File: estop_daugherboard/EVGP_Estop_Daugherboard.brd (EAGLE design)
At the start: 82.6 x 94.1 mm, 41 parts, among them J1 JST-XH-02-PIN-LONG-PAD, J2 JST-XH-02-PIN-LONG-PAD, J3 JST-XH-03-PIN-LONG-PAD, J4 JST-XH-03-PIN-LONG-PAD, J5 AVR_SPI_PROG_3X2PTH, J6 UX60-MB-5S8, J7 4_XH_JST, Q1 N_FET2, Q2 N_FET1, U1 NL27WZ08USG, U2 ATMEGA32U4-AU, X1 TSX-3225 16.0000MF18X-AC0

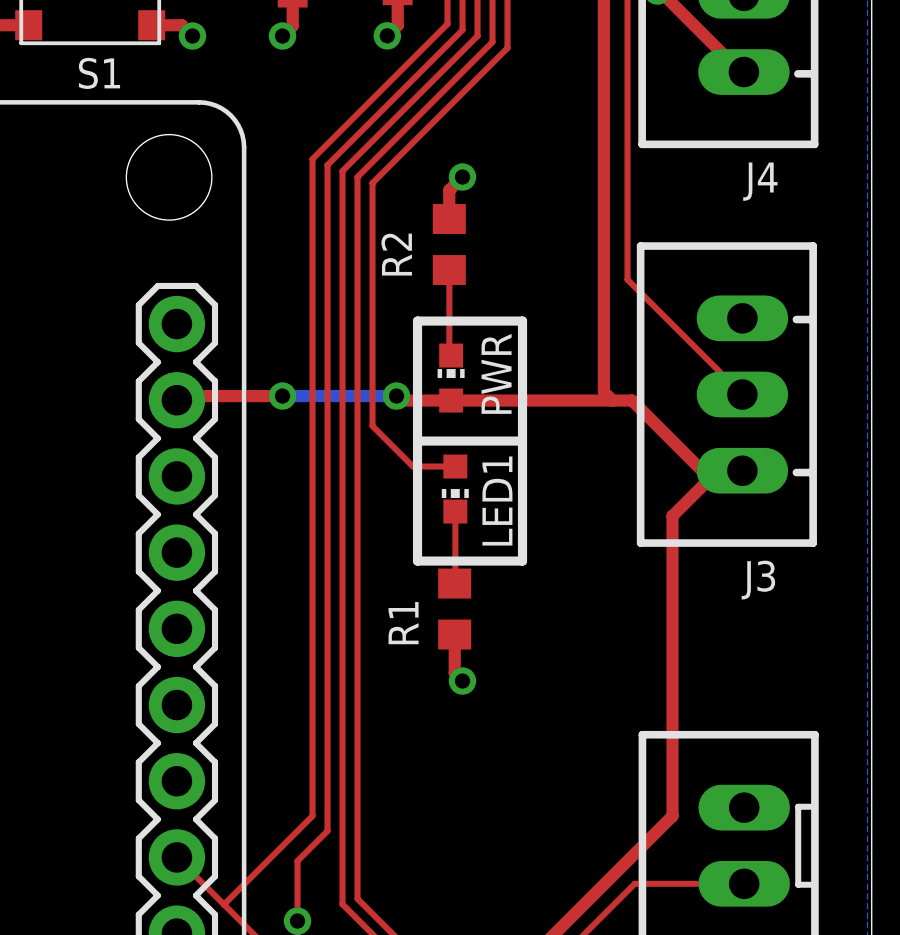
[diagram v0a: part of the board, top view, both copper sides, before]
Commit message: changed device led name
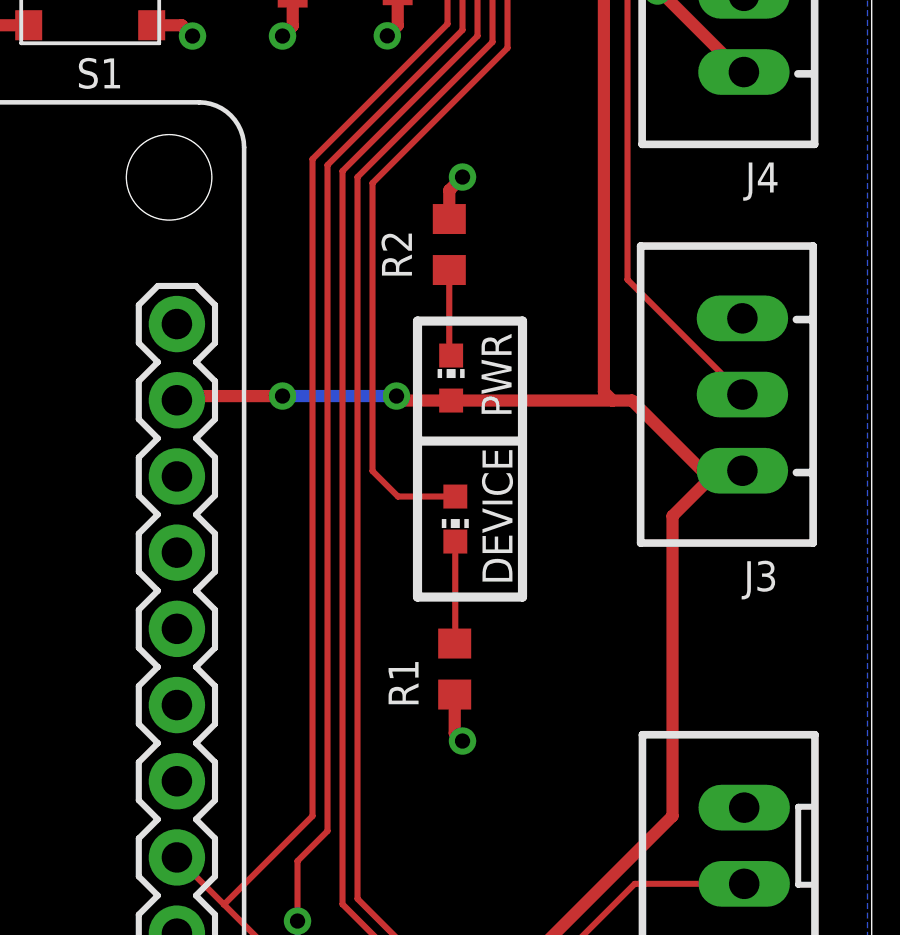
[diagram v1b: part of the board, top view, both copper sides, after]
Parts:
- removed LED1: BLUE, led:CHIP-LED0603
- added DEVICE: BLUE, led:CHIP-LED0603
- moved R1 2.00 mm to (74.7, 17.4)
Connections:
- net LED1: now also DEVICE.A; no longer LED1.A
- net N$6: now also DEVICE.C; no longer LED1.C
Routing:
- net LED1: track 30.7 -> 32.0 mm
- net N$6: track 2.41 -> 3.41 mm
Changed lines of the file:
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@@
 <wire x1="73.5" y1="29" x2="77" y2="29" width="0.3048" layer="21"/>
 <wire x1="77" y1="29" x2="77" y2="25" width="0.3048" layer="21"/>
-<wire x1="77" y1="25" x2="77" y2="21" width="0.3048" layer="21"/>
-<wire x1="77" y1="21" x2="73.5" y2="21" width="0.3048" layer="21"/>
-<wire x1="73.5" y1="21" x2="73.5" y2="25" width="0.3048" layer="21"/>
+<wire x1="77" y1="25" x2="77" y2="19.8" width="0.3048" layer="21"/>
+<wire x1="77" y1="19.8" x2="73.5" y2="19.8" width="0.3048" layer="21"/>
+<wire x1="73.5" y1="19.8" x2="73.5" y2="25" width="0.3048" layer="21"/>
 </plain>
 <attributes>
@@
 <attribute name="POPULARITY" value="26" x="74.62" y="27.1" size="1.778" layer="27" display="off"/>
 </element>
-<element name="LED1" library="led" library_urn="urn:adsk.eagle:library:259" package="CHIP-LED0603" package3d_urn="urn:adsk.eagle:package:15819/3" value="BLUE" x="74.76" y="23.4" smashed="yes" rot="R180">
-<attribute name="NAME" x="76.665" y="21.395" size="1" layer="25" font="vector" rot="R90"/>
-<attribute name="POPULARITY" value="26" x="74.76" y="23.4" size="1.778" layer="27" rot="R180" display="off"/>
+<element name="DEVICE" library="led" library_urn="urn:adsk.eagle:library:259" package="CHIP-LED0603" package3d_urn="urn:adsk.eagle:package:15819/3" value="BLUE" x="74.76" y="22.4" smashed="yes" rot="R180">
+<attribute name="NAME" x="76.665" y="20.195" size="1" layer="25" font="vector" rot="R90"/>
+<attribute name="POPULARITY" value="26" x="74.76" y="22.4" size="1.778" layer="27" rot="R180" display="off"/>
 </element>
 <element name="R3" library="rcl" library_urn="urn:adsk.eagle:library:334" package="R0603" package3d_urn="urn:adsk.eagle:package:23555/3" value="10k" x="62.99" y="45.34" smashed="yes">
@@
 <attribute name="SPICEPREFIX" value="R" x="183.62" y="90.32" size="1.778" layer="27" rot="R90" display="off"/>
 </element>
-<element name="R1" library="rcl" library_urn="urn:adsk.eagle:library:334" package="R0603" package3d_urn="urn:adsk.eagle:package:23555/3" value="330Ω" x="74.74" y="19.4" smashed="yes" rot="R90">
-<attribute name="NAME" x="73.535" y="18.105" size="1" layer="25" font="vector" rot="R90"/>
-<attribute name="POPULARITY" value="77" x="194.12" y="77.82" size="1.778" layer="27" rot="R90" display="off"/>
-<attribute name="SPICEPREFIX" value="R" x="194.12" y="77.82" size="1.778" layer="27" rot="R90" display="off"/>
+<element name="R1" library="rcl" library_urn="urn:adsk.eagle:library:334" package="R0603" package3d_urn="urn:adsk.eagle:package:23555/3" value="330Ω" x="74.74" y="17.4" smashed="yes" rot="R90">
+<attribute name="NAME" x="73.535" y="16.105" size="1" layer="25" font="vector" rot="R90"/>
+<attribute name="POPULARITY" value="77" x="194.12" y="75.82" size="1.778" layer="27" rot="R90" display="off"/>
+<attribute name="SPICEPREFIX" value="R" x="194.12" y="75.82" size="1.778" layer="27" rot="R90" display="off"/>
 </element>
 <element name="R8" library="rcl" library_urn="urn:adsk.eagle:library:334" package="R0603" package3d_urn="urn:adsk.eagle:package:23555/3" value="10kΩ" x="85.45" y="73.74" smashed="yes" rot="R180">
@@
 <wire x1="74.56" y1="33.36" x2="75" y2="33.8" width="0.4064" layer="1"/>
 <via x="75" y="33.8" extent="1-16" drill="0.508"/>
-<wire x1="74.74" y1="18.55" x2="74.74" y2="17.26" width="0.4064" layer="1"/>
-<wire x1="74.74" y1="17.26" x2="75" y2="17" width="0.4064" layer="1"/>
-<via x="75" y="17" extent="1-16" drill="0.508"/>
+<wire x1="74.74" y1="16.55" x2="74.74" y2="15.26" width="0.4064" layer="1"/>
+<wire x1="74.74" y1="15.26" x2="75" y2="15" width="0.4064" layer="1"/>
+<via x="75" y="15" extent="1-16" drill="0.508"/>
 <wire x1="77.05" y1="52.26" x2="77.05" y2="51.55" width="0.4064" layer="1"/>
 <wire x1="77.05" y1="51.55" x2="76.5" y2="51" width="0.4064" layer="1"/>
@@
 </signal>
 <signal name="N$6">
-<contactref element="LED1" pad="C"/>
+<contactref element="DEVICE" pad="C"/>
 <contactref element="R1" pad="2"/>
-<wire x1="74.76" y1="22.65" x2="74.76" y2="20.27" width="0.2032" layer="1"/>
-<wire x1="74.76" y1="20.27" x2="74.74" y2="20.25" width="0.2032" layer="1"/>
+<wire x1="74.76" y1="21.65" x2="74.76" y2="18.27" width="0.2032" layer="1"/>
+<wire x1="74.76" y1="18.27" x2="74.74" y2="18.25" width="0.2032" layer="1"/>
 </signal>
 <signal name="LED1">
-<contactref element="LED1" pad="A"/>
+<contactref element="DEVICE" pad="A"/>
 <contactref element="U2" pad="22"/>
-<wire x1="74.76" y1="24.15" x2="73.35" y2="24.15" width="0.2032" layer="1"/>
-<wire x1="73.35" y1="24.15" x2="72" y2="25.5" width="0.2032" layer="1"/>
+<wire x1="74.76" y1="23.15" x2="72.85" y2="23.15" width="0.2032" layer="1"/>
+<wire x1="72.85" y1="23.15" x2="72" y2="24" width="0.2032" layer="1"/>
 <wire x1="75.25" y1="49.35" x2="75.25" y2="50.46" width="0.2032" layer="1"/>
-<wire x1="72" y1="25.5" x2="72" y2="33.6" width="0.2032" layer="1"/>
+<wire x1="72" y1="24" x2="72" y2="33.6" width="0.2032" layer="1"/>
 <wire x1="72" y1="33.6" x2="76.5" y2="38.1" width="0.2032" layer="1"/>
 <wire x1="76.5" y1="38.1" x2="76.5" y2="48.1" width="0.2032" layer="1"/>

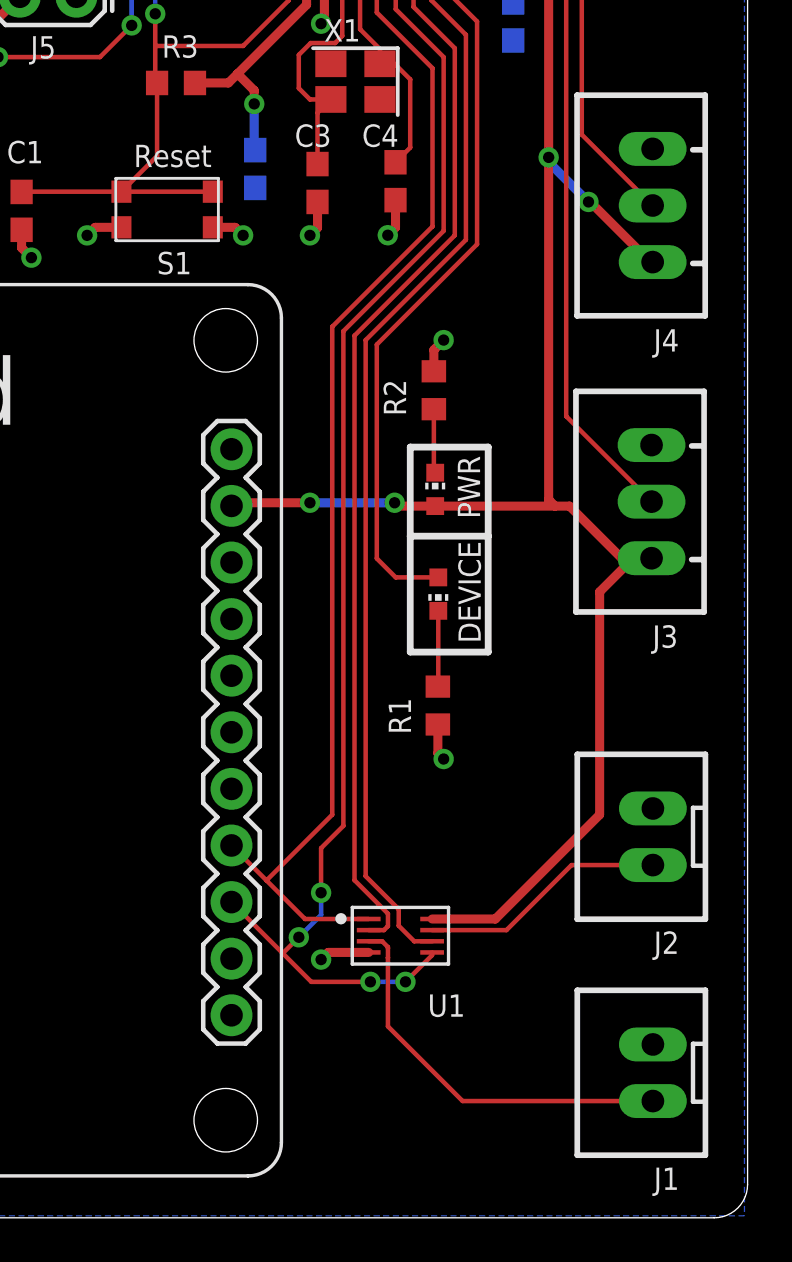
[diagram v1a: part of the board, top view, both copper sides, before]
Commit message: changed device led name
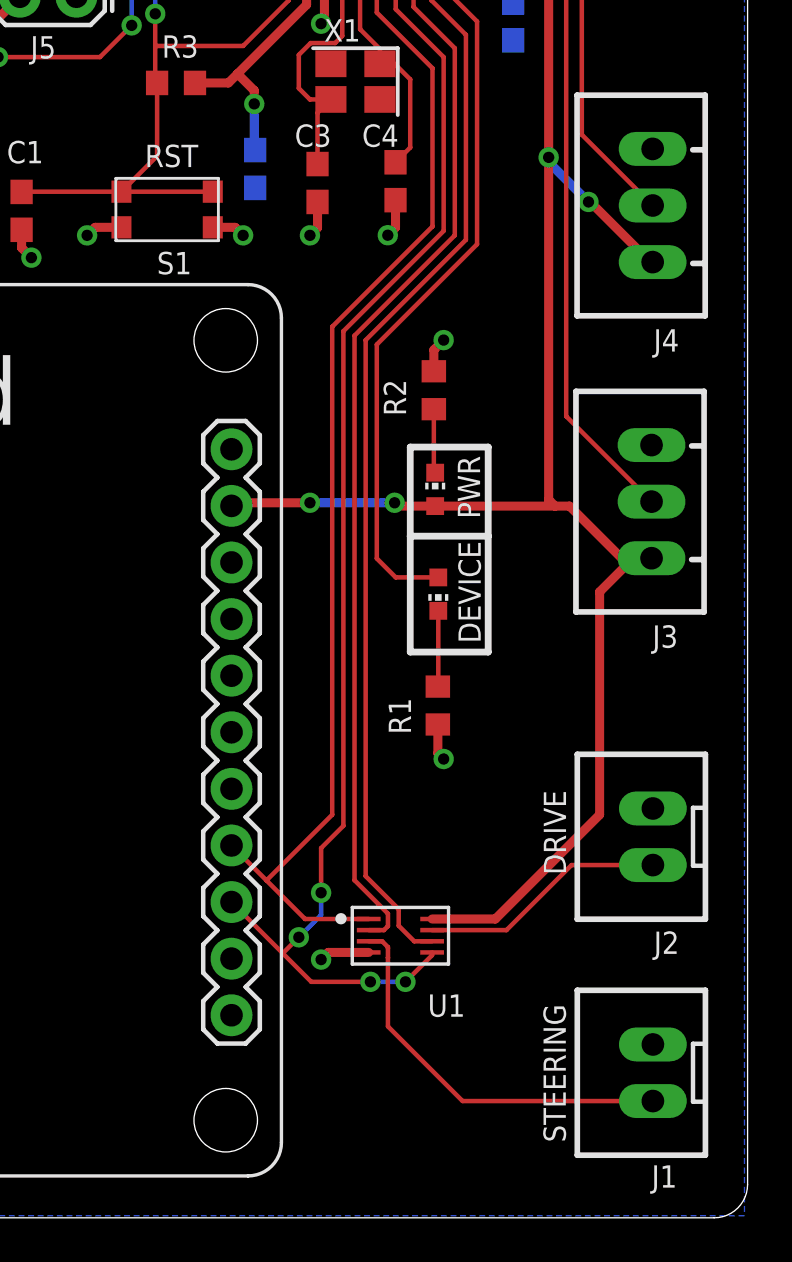
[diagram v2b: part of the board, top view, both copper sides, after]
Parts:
- J1: value JST-XH-02-PIN-LONG-PAD -> STEERING
- J2: value JST-XH-02-PIN-LONG-PAD -> DRIVE
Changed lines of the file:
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@@
 </element>
 <element name="S1" library="RoboJackets-Switches" package="KMR2" value="KMR2" x="62.59" y="39.66" smashed="yes" rot="R180">
-<attribute name="FUNCTION" value="Reset" x="61.09" y="41.565" size="1" layer="25" font="vector"/>
+<attribute name="FUNCTION" value="RST" x="61.59" y="41.565" size="1" layer="25" font="vector"/>
 <attribute name="NAME" x="62.13" y="36.755" size="1" layer="25" font="vector"/>
 </element>
@@
 <attribute name="NAME" x="69.64" y="47.2" size="1" layer="25" font="vector"/>
 </element>
-<element name="J2" library="Rembrandt Electronics - JST XH Connectors v1-0" package="JST-XH-02-PACKAGE-LONG-PAD" value="JST-XH-02-PIN-LONG-PAD" x="84.39" y="11.51" smashed="yes" rot="R90">
+<element name="J2" library="Rembrandt Electronics - JST XH Connectors v1-0" package="JST-XH-02-PACKAGE-LONG-PAD" value="DRIVE" x="84.39" y="11.51" smashed="yes" rot="R90">
 <attribute name="NAME" x="84.43" y="6.255" size="1" layer="25" font="vector"/>
+<attribute name="VALUE" x="80.4925" y="9.7975" size="1" layer="25" font="vector" rot="R90"/>
 </element>
-<element name="J1" library="Rembrandt Electronics - JST XH Connectors v1-0" package="JST-XH-02-PACKAGE-LONG-PAD" value="JST-XH-02-PIN-LONG-PAD" x="84.39" y="0.92" smashed="yes" rot="R90">
-<attribute name="NAME" x="84.43" y="-4.335" size="1" layer="25" font="vector"/>
+<element name="J1" library="Rembrandt Electronics - JST XH Connectors v1-0" package="JST-XH-02-PACKAGE-LONG-PAD" value="STEERING" x="84.39" y="0.92" smashed="yes" rot="R90">
+<attribute name="NAME" x="84.33" y="-4.235" size="1" layer="25" font="vector"/>
+<attribute name="VALUE" x="80.4825" y="-2.2025" size="1" layer="25" font="vector" rot="R90"/>
 </element>
 <element name="J4" library="Rembrandt Electronics - JST XH Connectors v1-0" package="JST-XH-03-PACKAGE-LONG-PAD" value="JST-XH-03-PIN-LONG-PAD" x="84.38" y="39.84" smashed="yes" rot="R90">

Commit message: Changed the library name, added 555 to library, implemented into both 'normal' and 'led' boards
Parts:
- J1, J2: device Rembrandt Electronics - JST XH Connectors v1-0:JST-XH-02-PACKAGE-LONG-PAD -> EVGP_Estop_Daughterboard:JST-XH-02-PACKAGE-LONG-PAD
- J3, J4: device Rembrandt Electronics - JST XH Connectors v1-0:JST-XH-03-PACKAGE-LONG-PAD -> EVGP_Estop_Daughterboard:JST-XH-03-PACKAGE-LONG-PAD
- J7: device Rembrandt Electronics - JST XH Connectors v1-0:JST-XH-04-PACKAGE-LONG-PAD -> EVGP_Estop_Daughterboard:JST-XH-04-PACKAGE-LONG-PAD
- Q1, Q2: device Daughterboard-Stuff:SOT-363 -> EVGP_Estop_Daughterboard:SOT-363
- U1: device Daughterboard-Stuff:US8_2P40X2P10 -> EVGP_Estop_Daughterboard:US8_2P40X2P10
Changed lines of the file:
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@@
 <drawing>
 <settings>
-<setting alwaysvectorfont="no"/>
+<setting alwaysvectorfont="yes"/>
 <setting verticaltext="up"/>
 </settings>
@@
 <attribute name="PINS" value="5" x="-41.67" y="61.49" size="1.778" layer="27" rot="R270" display="off"/>
 </element>
-<element name="J7" library="Rembrandt Electronics - JST XH Connectors v1-0" package="JST-XH-04-PACKAGE-LONG-PAD" value="4_XH_JST" x="79.32" y="84.83" smashed="yes" rot="R180">
+<element name="J7" library="EVGP_Estop_Daughterboard" package="JST-XH-04-PACKAGE-LONG-PAD" value="4_XH_JST" x="79.32" y="84.83" smashed="yes" rot="R180">
 <attribute name="NAME" x="72.525" y="84.13" size="1" layer="25" font="vector" rot="R90"/>
 </element>
@@
 <attribute name="NAME" x="70.44" y="55.745" size="1" layer="25" font="vector"/>
 </element>
-<element name="U1" library="Daughterboard-Stuff" package="US8_2P40X2P10" value="NL27WZ08USG" x="73.06" y="7.07" smashed="yes">
+<element name="U1" library="EVGP_Estop_Daughterboard" package="US8_2P40X2P10" value="NL27WZ08USG" x="73.06" y="7.07" smashed="yes">
 <attribute name="MANUFACTURER_PART_NUMBER" value="NL27WZ08USG" x="121.32" y="-116.12" size="1.778" layer="27" display="off"/>
 <attribute name="NAME" x="74.2834" y="3.435" size="1" layer="25" font="vector"/>
 <attribute name="VENDOR" value="ON Semiconductor" x="121.32" y="-116.12" size="1.778" layer="27" display="off"/>
 </element>
-<element name="Q2" library="Daughterboard-Stuff" package="SOT-363" value="N_FET1" x="84.65" y="78.14" smashed="yes">
+<element name="Q2" library="EVGP_Estop_Daughterboard" package="SOT-363" value="N_FET1" x="84.65" y="78.14" smashed="yes">
 <attribute name="MANUFACTURER_PART_NUMBER" value="BSS84DW7F" x="149.42" y="-46.32" size="1.778" layer="27" display="off"/>
 <attribute name="NAME" x="84.3734" y="80.005" size="1" layer="25" font="vector"/>
 <attribute name="VENDOR" value="Diodes Inc" x="149.42" y="-46.32" size="1.778" layer="27" display="off"/>
 </element>
-<element name="Q1" library="Daughterboard-Stuff" package="SOT-363" value="N_FET2" x="77.5" y="78.04" smashed="yes">
+<element name="Q1" library="EVGP_Estop_Daughterboard" package="SOT-363" value="N_FET2" x="77.5" y="78.04" smashed="yes">
 <attribute name="MANUFACTURER_PART_NUMBER" value="BSS84DW7F" x="148.62" y="-46.42" size="1.778" layer="27" display="off"/>
 <attribute name="NAME" x="76.7234" y="79.905" size="1" layer="25" font="vector"/>
@@
 <attribute name="NAME" x="69.64" y="47.2" size="1" layer="25" font="vector"/>
 </element>
-<element name="J2" library="Rembrandt Electronics - JST XH Connectors v1-0" package="JST-XH-02-PACKAGE-LONG-PAD" value="DRIVE" x="84.39" y="11.51" smashed="yes" rot="R90">
+<element name="J2" library="EVGP_Estop_Daughterboard" package="JST-XH-02-PACKAGE-LONG-PAD" value="DRIVE" x="84.39" y="11.51" smashed="yes" rot="R90">
 <attribute name="NAME" x="84.43" y="6.255" size="1" layer="25" font="vector"/>
 <attribute name="VALUE" x="80.4925" y="9.7975" size="1" layer="25" font="vector" rot="R90"/>
 </element>
-<element name="J1" library="Rembrandt Electronics - JST XH Connectors v1-0" package="JST-XH-02-PACKAGE-LONG-PAD" value="STEERING" x="84.39" y="0.92" smashed="yes" rot="R90">
+<element name="J1" library="EVGP_Estop_Daughterboard" package="JST-XH-02-PACKAGE-LONG-PAD" value="STEERING" x="84.39" y="0.92" smashed="yes" rot="R90">
 <attribute name="NAME" x="84.33" y="-4.235" size="1" layer="25" font="vector"/>
 <attribute name="VALUE" x="80.4825" y="-2.2025" size="1" layer="25" font="vector" rot="R90"/>
 </element>
-<element name="J4" library="Rembrandt Electronics - JST XH Connectors v1-0" package="JST-XH-03-PACKAGE-LONG-PAD" value="JST-XH-03-PIN-LONG-PAD" x="84.38" y="39.84" smashed="yes" rot="R90">
+<element name="J4" library="EVGP_Estop_Daughterboard" package="JST-XH-03-PACKAGE-LONG-PAD" value="JST-XH-03-PIN-LONG-PAD" x="84.38" y="39.84" smashed="yes" rot="R90">
 <attribute name="NAME" x="84.42" y="33.285" size="1" layer="25" font="vector"/>
 </element>
-<element name="J3" library="Rembrandt Electronics - JST XH Connectors v1-0" package="JST-XH-03-PACKAGE-LONG-PAD" value="JST-XH-03-PIN-LONG-PAD" x="84.33" y="26.55" smashed="yes" rot="R90">
+<element name="J3" library="EVGP_Estop_Daughterboard" package="JST-XH-03-PACKAGE-LONG-PAD" value="JST-XH-03-PIN-LONG-PAD" x="84.33" y="26.55" smashed="yes" rot="R90">
 <attribute name="NAME" x="84.37" y="19.995" size="1" layer="25" font="vector"/>
 </element>
